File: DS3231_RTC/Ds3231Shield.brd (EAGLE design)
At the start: 39.7 x 26.7 mm, 5 parts

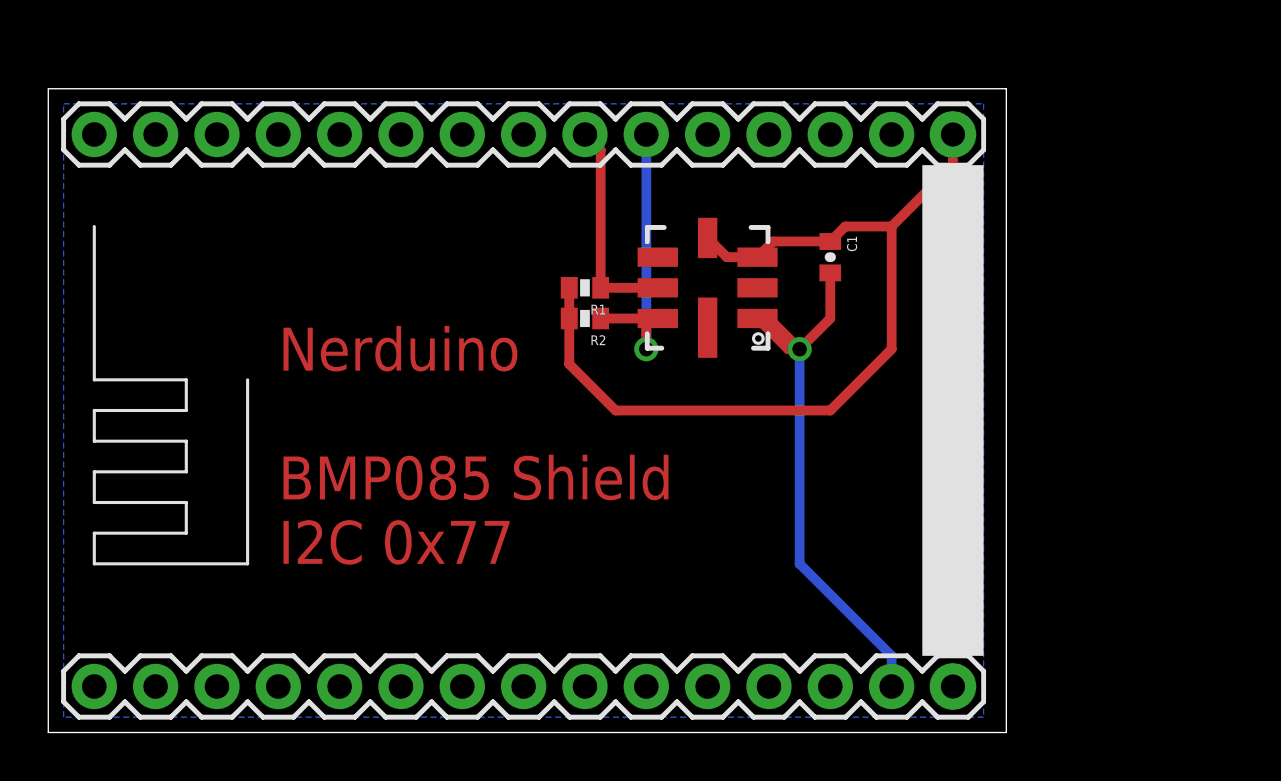
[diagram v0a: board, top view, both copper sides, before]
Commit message: Updated BMP180 symbol Removed BMP085 shield (redundant) Added DS3231 RTC Shield Added LTC2495 ADC Shield Added chip data sheets for each shield
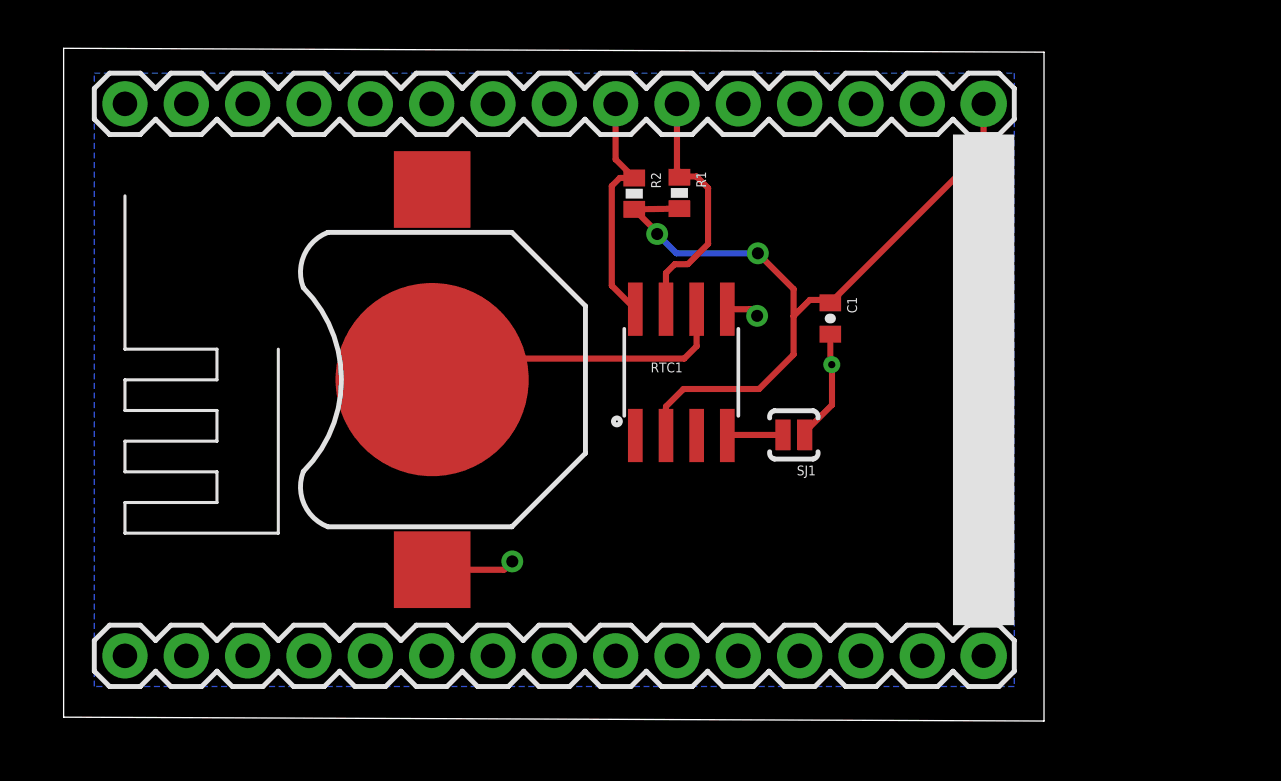
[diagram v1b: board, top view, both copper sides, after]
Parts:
- removed U$2: BMP085, SparkFun:BMP085
- added BAT1: (no value), SparkFun-Electromechanical:BATTCON_12MM
- added RTC1: DS3231M, SparkFun-DigitalIC:SOIC8
- added SJ1: SOLDERJUMPERNO, SparkFun:SJ_2S-NO
- moved R2 5.56 mm to (23.6, 21.7), turned to 270 degrees
- moved R1 5.54 mm to (25.5, 21.7), turned to 270 degrees
- moved C1 2.54 mm to (31.8, 16.5)
- moved U$1 1.80 mm to (20.3, 7.62)
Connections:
- new net N$1: BAT1.GND, RTC1.6
- new net N$4: RTC1.4, SJ1.2
- net 3.3V: now also RTC1.2; no longer U$2.3, U$2.4
- net GND: now also BAT1.PWR@1, RTC1.5, SJ1.1; no longer U$2.1
- net N$2: now also RTC1.8, U$1.22; no longer U$1.21, U$2.7
- net N$3: now also RTC1.7, U$1.21; no longer U$1.22, U$2.6
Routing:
- net GND: track 23.8 -> 10.1 mm, vias 1 -> 3
- net N$1: track 0.00 -> 13.1 mm
- net 3.3V: track 36.8 -> 32.7 mm, vias 0 -> 2
- net N$2: track 12.5 -> 9.96 mm, vias 1 -> 0
- net N$4: track 0.00 -> 2.33 mm
- net N$3: track 8.98 -> 10.5 mm
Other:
- board size 39.7 x 26.7 mm -> 40.6 x 27.9 mm
- board text removed: "Nerduino BMP085 Shield I2C 0x77"

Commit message: Added OLED Shield Added LiPo Battery Charger Shield Updated outlines of all shields to match the cutout of the nodemcu board
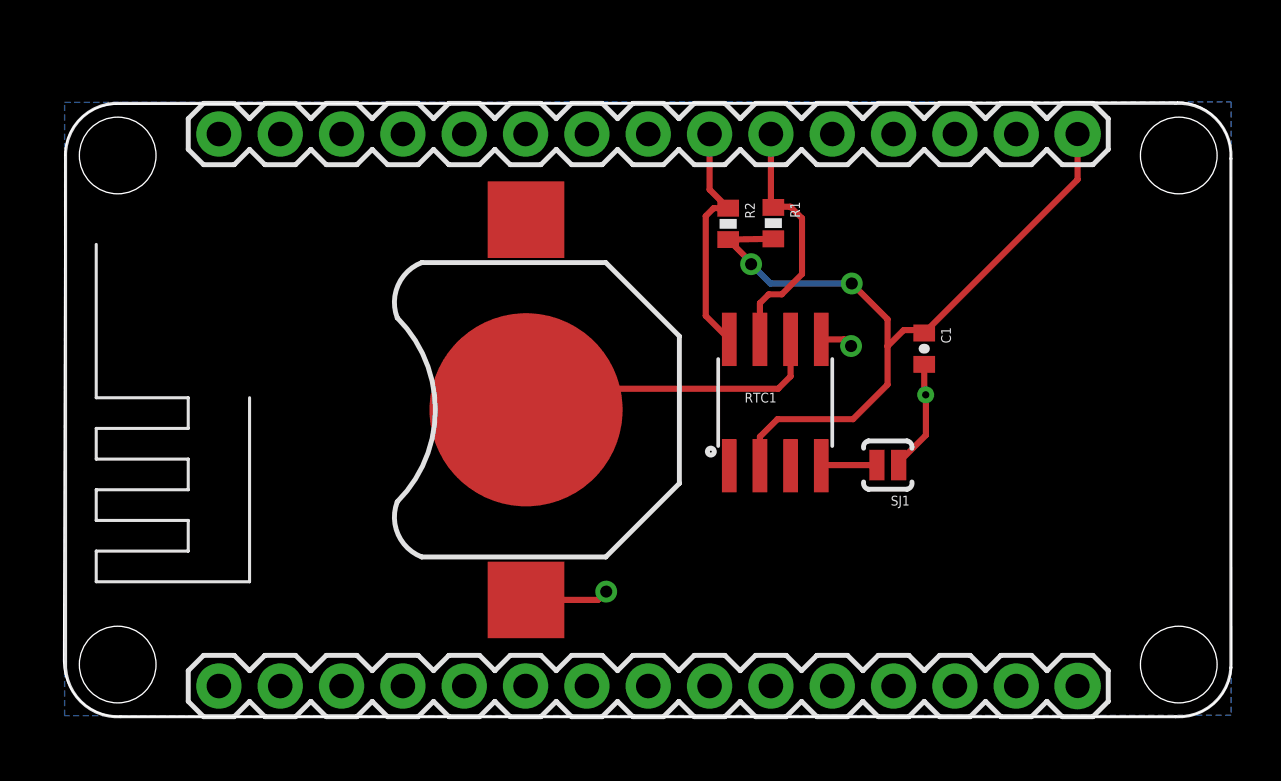
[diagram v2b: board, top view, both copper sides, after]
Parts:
- moved SJ1 4.09 mm to (34.1, 10.4)
- moved C1 4.09 mm to (35.6, 15.3)
- moved R1 4.09 mm to (29.4, 20.5)
- moved R2 4.09 mm to (27.5, 20.4)
- moved RTC1 4.09 mm to (29.5, 13.0)
- moved U$1 4.09 mm to (24.2, 6.37)
- moved BAT1 4.09 mm to (19.1, 12.7)
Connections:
- net GND: now also U$1.10, U$1.17, U$1.24
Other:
- board size 40.6 x 27.9 mm -> 48.4 x 25.5 mm
- board text added: "NERDUINO RealTimeClock Shield I2C 0x? www.nerduino.com"

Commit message: Updated the i2c pins to all shields to use d11/d12  as these pins will have dual use with the upcoming wifimcu Added FM24W256  Fram shield Added X95840 Digital potentiometer Shield Added AD5696 DAC Shield
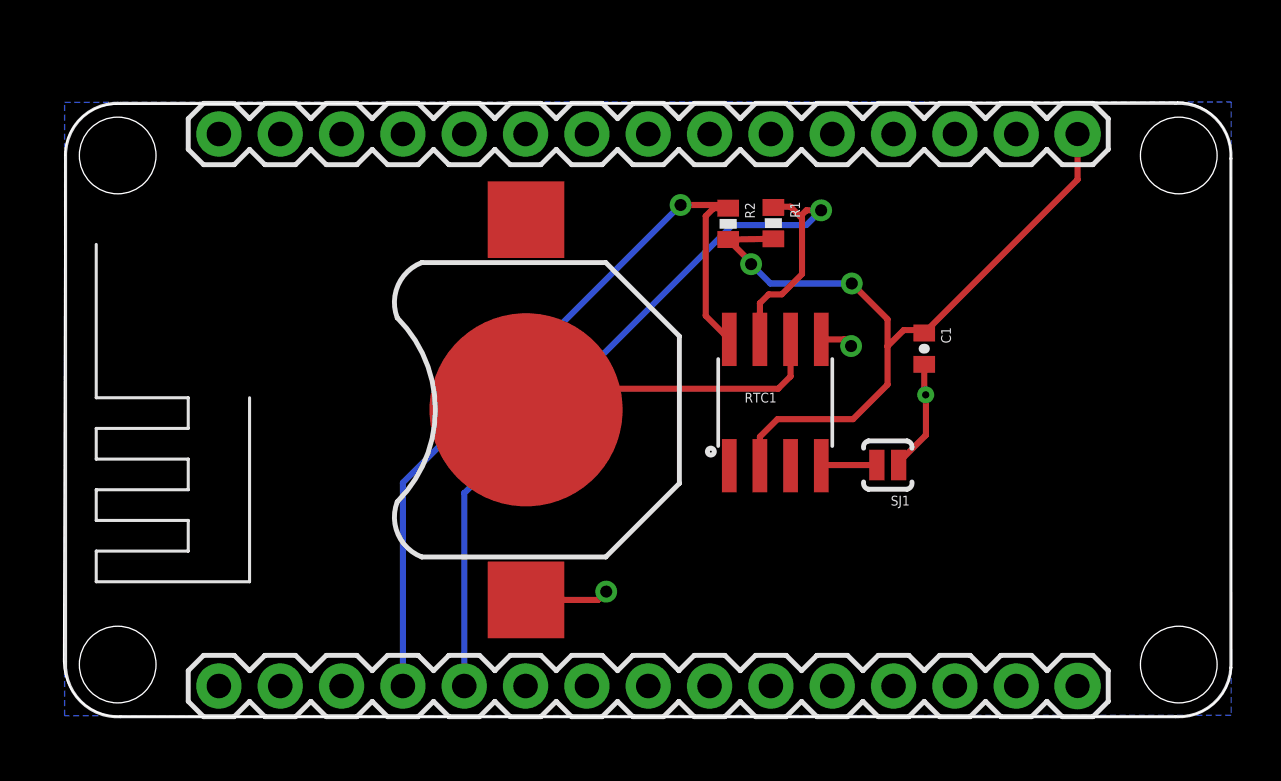
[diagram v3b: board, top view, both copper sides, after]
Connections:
- net GND: no longer U$1.24
- net N$2: now also U$1.4; no longer U$1.22
- net N$3: now also U$1.5; no longer U$1.21
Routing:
- net N$3: track 10.5 -> 36.2 mm, vias 0 -> 1
- net N$2: track 9.96 -> 33.3 mm, vias 0 -> 1
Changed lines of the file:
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@@
 <wire x1="22.56" y1="5.2" x2="22.64" y2="5.12" width="0.254" layer="16"/>
 <contactref element="U$1" pad="10"/>
-<contactref element="U$1" pad="24"/>
 <contactref element="U$1" pad="17"/>
 </signal>
@@
 <signal name="N$2">
 <contactref element="R2" pad="1"/>
-<contactref element="U$1" pad="22"/>
 <contactref element="RTC1" pad="8"/>
-<wire x1="26.75" y1="24.15" x2="26.75" y2="21.85" width="0.254" layer="1"/>
-<wire x1="26.75" y1="21.85" x2="27.52" y2="21.08" width="0.254" layer="1"/>
 <wire x1="27.52" y1="21.08" x2="26.92" y2="21.08" width="0.254" layer="1"/>
 <wire x1="26.92" y1="21.08" x2="26.59" y2="20.75" width="0.254" layer="1"/>
 <wire x1="26.59" y1="20.75" x2="26.59" y2="16.6212" width="0.254" layer="1"/>
 <wire x1="26.59" y1="16.6212" x2="27.565" y2="15.6462" width="0.254" layer="1"/>
+<contactref element="U$1" pad="4"/>
+<wire x1="14.05" y1="1.29" x2="14.05" y2="9.71" width="0.254" layer="16"/>
+<wire x1="14.05" y1="9.71" x2="25.55" y2="21.21" width="0.254" layer="16"/>
+<via x="25.55" y="21.21" extent="1-16" drill="0.5"/>
+<wire x1="25.55" y1="21.21" x2="27.39" y2="21.21" width="0.254" layer="1"/>
+<wire x1="27.39" y1="21.21" x2="27.52" y2="21.08" width="0.254" layer="1"/>
 </signal>
 <signal name="N$3">
 <contactref element="R1" pad="1"/>
-<contactref element="U$1" pad="21"/>
 <contactref element="RTC1" pad="7"/>
-<wire x1="29.29" y1="24.15" x2="29.29" y2="21.21" width="0.254" layer="1"/>
 <wire x1="29.29" y1="21.21" x2="29.39" y2="21.11" width="0.254" layer="1"/>
 <wire x1="28.835" y1="15.6462" x2="28.835" y2="17.145" width="0.254" layer="1"/>
@@
 <wire x1="29.74" y1="17.51" x2="30.58" y2="18.35" width="0.254" layer="1"/>
 <wire x1="30.58" y1="18.35" x2="30.58" y2="20.66" width="0.254" layer="1"/>
-<wire x1="30.58" y1="20.66" x2="30.1" y2="21.14" width="0.254" layer="1"/>
+<wire x1="30.58" y1="20.66" x2="30.505" y2="20.735" width="0.254" layer="1"/>
+<wire x1="30.505" y1="20.735" x2="30.1" y2="21.14" width="0.254" layer="1"/>
 <wire x1="30.1" y1="21.14" x2="29.42" y2="21.14" width="0.254" layer="1"/>
 <wire x1="29.42" y1="21.14" x2="29.39" y2="21.11" width="0.254" layer="1"/>
+<contactref element="U$1" pad="5"/>
+<wire x1="16.59" y1="1.29" x2="16.59" y2="9.28" width="0.254" layer="16"/>
+<wire x1="16.59" y1="9.28" x2="27.69" y2="20.38" width="0.254" layer="16"/>
+<wire x1="27.69" y1="20.38" x2="30.76" y2="20.38" width="0.254" layer="16"/>
+<wire x1="30.76" y1="20.38" x2="31.37" y2="20.99" width="0.254" layer="16"/>
+<via x="31.37" y="20.99" extent="1-16" drill="0.5"/>
+<wire x1="31.37" y1="20.99" x2="30.76" y2="20.99" width="0.254" layer="1"/>
+<wire x1="30.76" y1="20.99" x2="30.505" y2="20.735" width="0.254" layer="1"/>
 </signal>
 <signal name="N$1">
